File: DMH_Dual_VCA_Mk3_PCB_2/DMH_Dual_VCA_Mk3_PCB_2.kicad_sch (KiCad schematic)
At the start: 0 parts

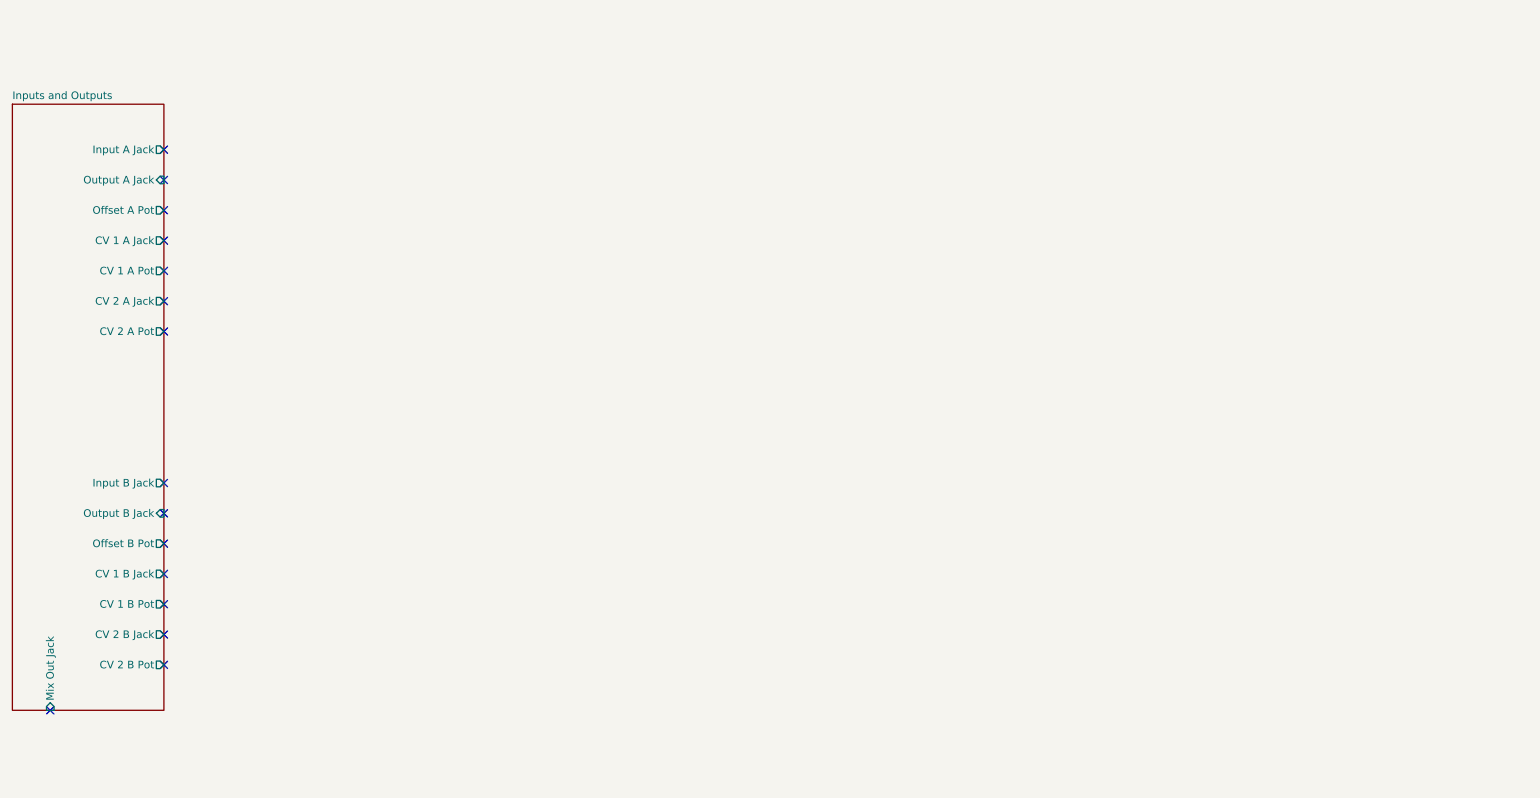
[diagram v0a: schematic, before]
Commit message: Synced PCB 1 and 2 schematics
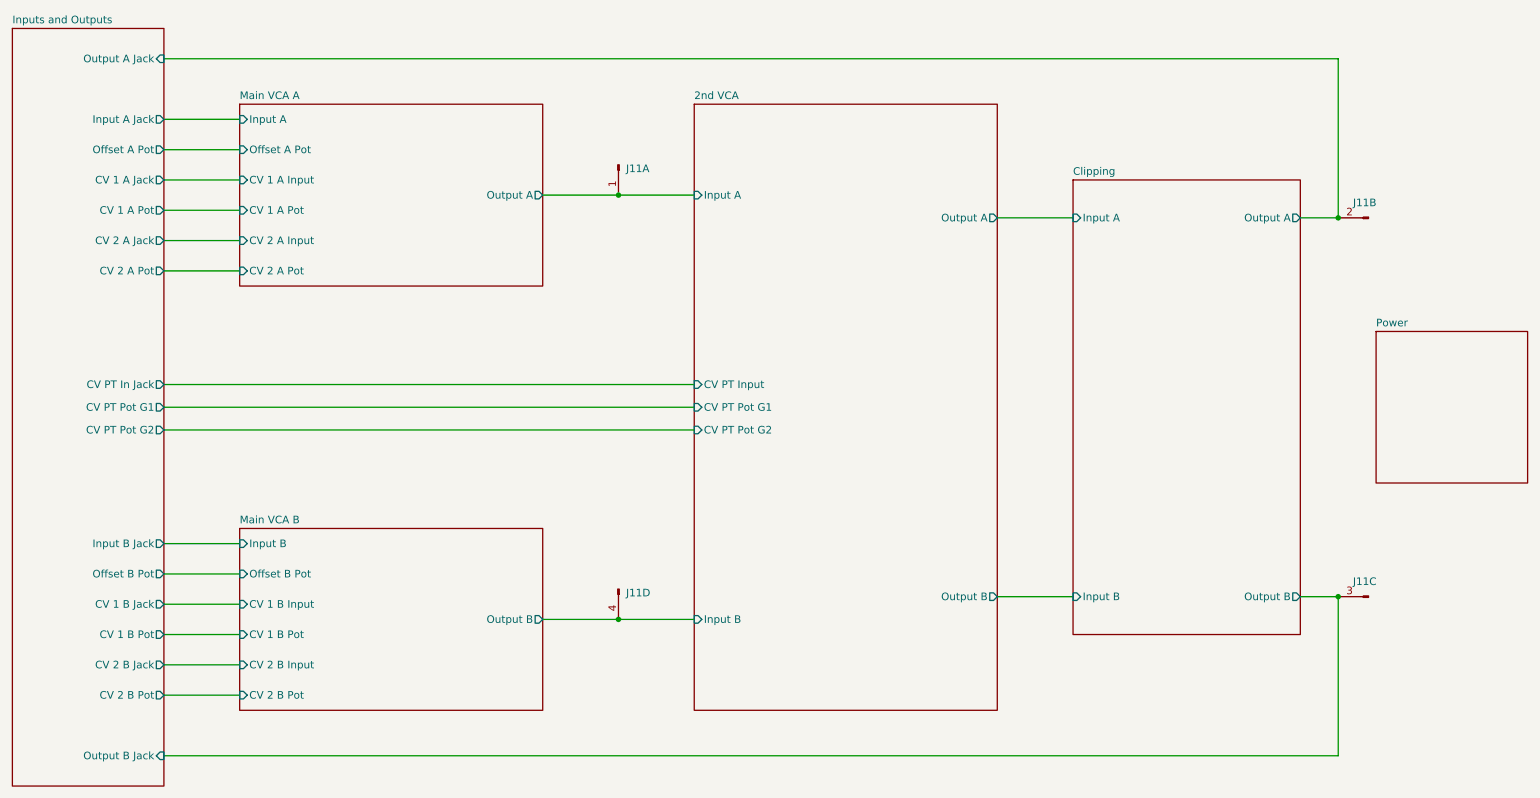
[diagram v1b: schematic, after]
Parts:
- added J11: Conn_01x04_PinHeader, Connector_PinSocket_2.54mm:PinSocket_1x04_P2.54mm_Vertical, symbol SynthStuff:Conn_01x04_PinHeader
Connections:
- new net 2nd VCA/Input A: J11.1 (Pin_1)
- new net 2nd VCA/Input B: J11.4 (Pin_4)
- new net Clipping/Output A: J11.2 (Pin_2)
- new net Clipping/Output B: J11.3 (Pin_3)
- no-connect marks 15 -> 0
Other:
- added sheet 2nd VCA (2nc_VCA.kicad_sch)
- added sheet Clipping (Clipping.kicad_sch)
- added sheet Main VCA A (Core_Circuit_A.kicad_sch)
- added sheet Main VCA B (Core_Circuit_B.kicad_sch)
- added sheet Power (Power.kicad_sch)
- sheet Inputs and Outputs ports: added CV PT In Jack, CV PT Pot G1, CV PT Pot G2; removed Mix Out Jack
